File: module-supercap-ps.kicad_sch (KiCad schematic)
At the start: 39 parts, among them J5 HB-PH3-25415PB2GOP, J6 HB-PH3-25414PB2GOP, Q3 FDV301N, Q4 BC817, U2 USBLC6-2SC6, U3 CD4011UBM, U4 SI1865DDL, U5 ME2108A50M, U6 TLC555DTR

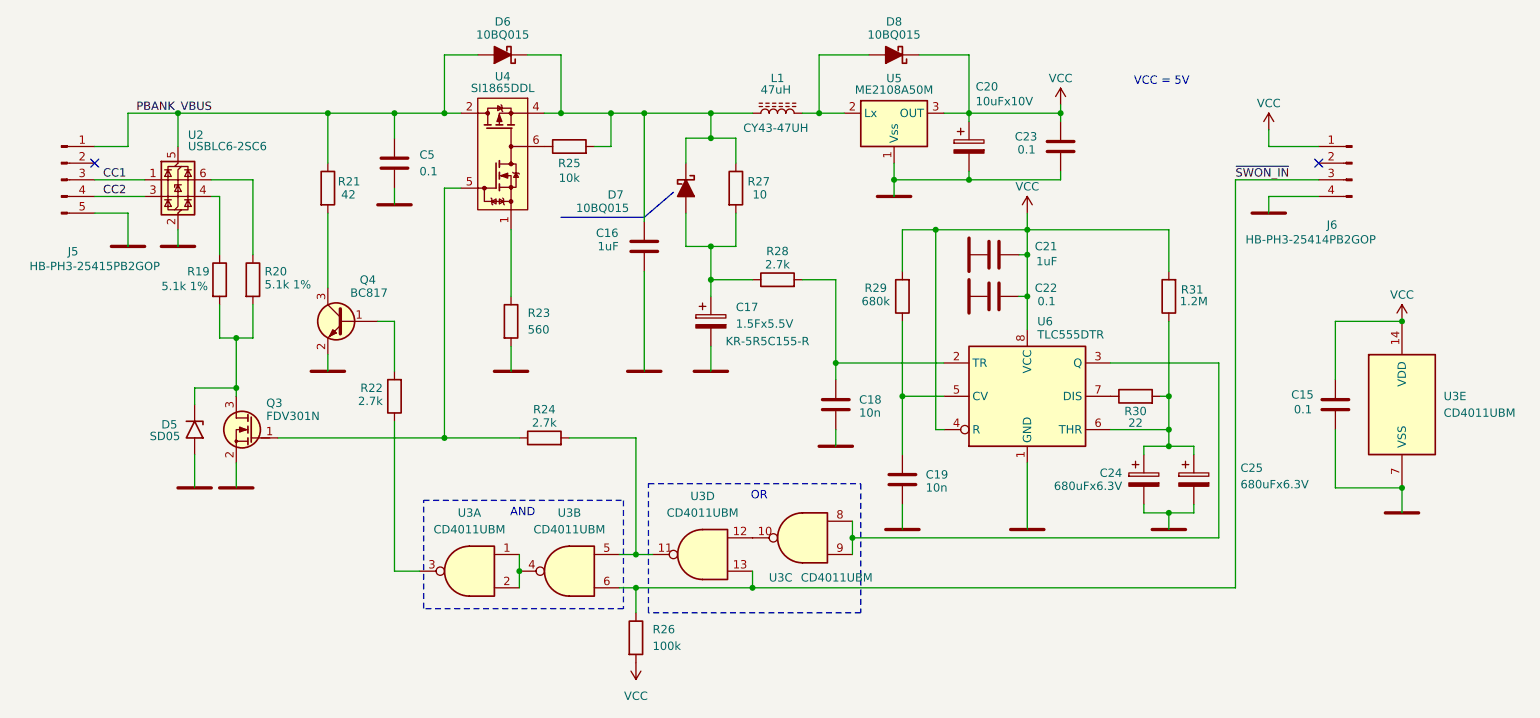
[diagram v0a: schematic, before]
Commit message: Работа со схемой модуля
Частичная отрисовка и назначение посадочных мест субмодуля питания от PowerBank. *Работа продолжается*.
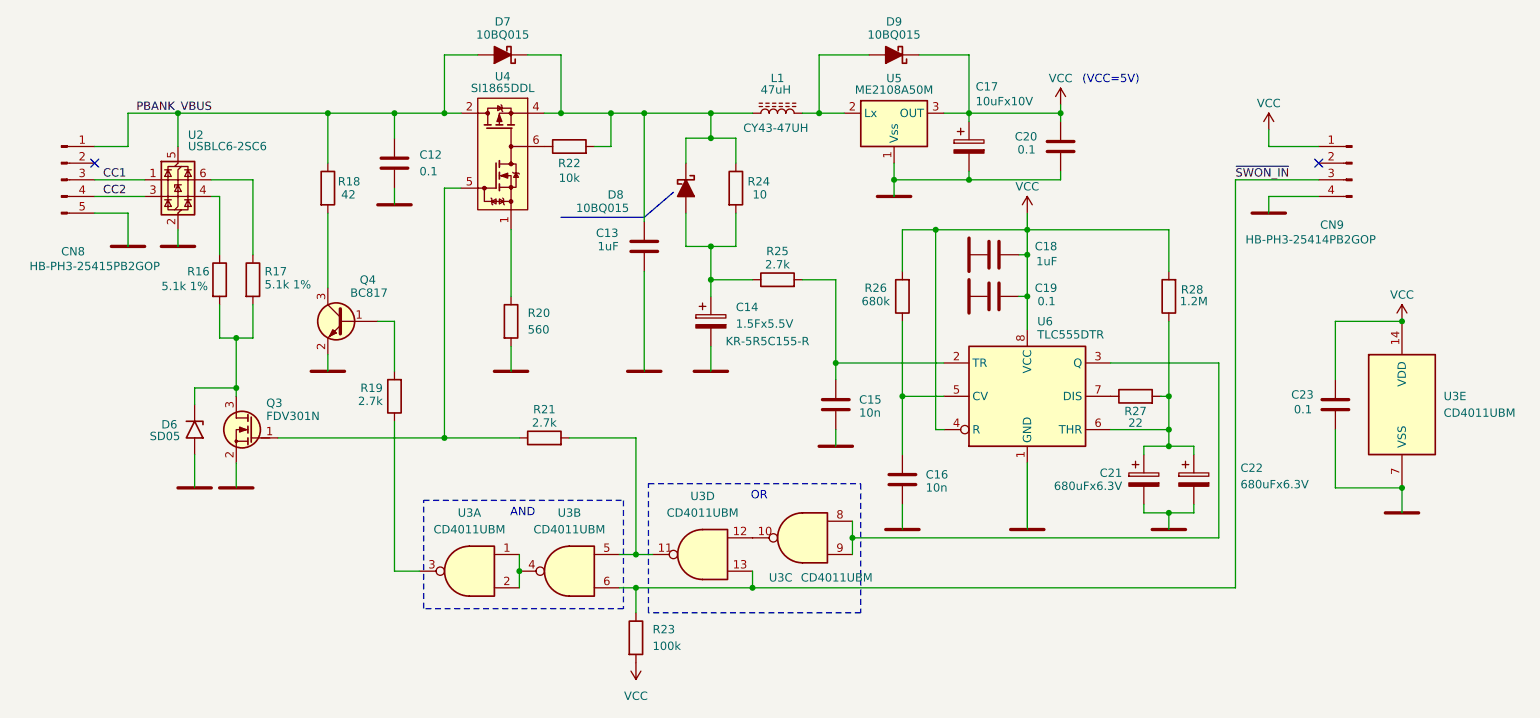
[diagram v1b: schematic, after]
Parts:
- renumbered C5 to C12, C16 to C13, C17 to C14, C18 to C15, C19 to C16, C20 to C17, C21 to C18, C22 to C19, C23 to C20, C24 to C21, C25 to C22, C15 to C23, J5 to CN8, J6 to CN9, D5 to D6, D6 to D7, D7 to D8, D8 to D9, R19 to R16, R20 to R17, R21 to R18, R22 to R19, R23 to R20, R24 to R21, R25 to R22, R26 to R23, R27 to R24, R28 to R25, R29 to R26, R30 to R27, R31 to R28
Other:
- note added: "(VCC=5V)"
- note removed: "VCC = 5V"
